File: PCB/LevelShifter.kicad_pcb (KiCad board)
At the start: 2 copper layers, 122.7 x 104.9 mm, 110 parts, among them J1 POWER, J10 M2, J11 M1, J12 Selector, J13 M0, J14 M_FEED, J15 M_FEED, J16 M_FEED, J17 Selector, J18 OUTPUT, J19 OUT0, J2 INPUT, J20 OUT1, J21 OUT2, J22 OUT3, J23 IN0, J24 IN1, J25 IN2, J26 IN3, J27 ROBOT, J28 ZIF, J3 ANALOG0, J4 ANALOG1, J5 ANALOG2, J6 ANALOG3, J7 DE9_Plug_MountingHoles, J8 SPECIAL, J9 RESET, Q1 IRF540N, Q2 IRF540N, Q3 IRF540N, U1 LM324A, U10 PC817, U2 MAX232, U3 PC817, U4 PC817, U5 PC817, U6 PC817, U7 PC817, U8 PC817, U9 PC817

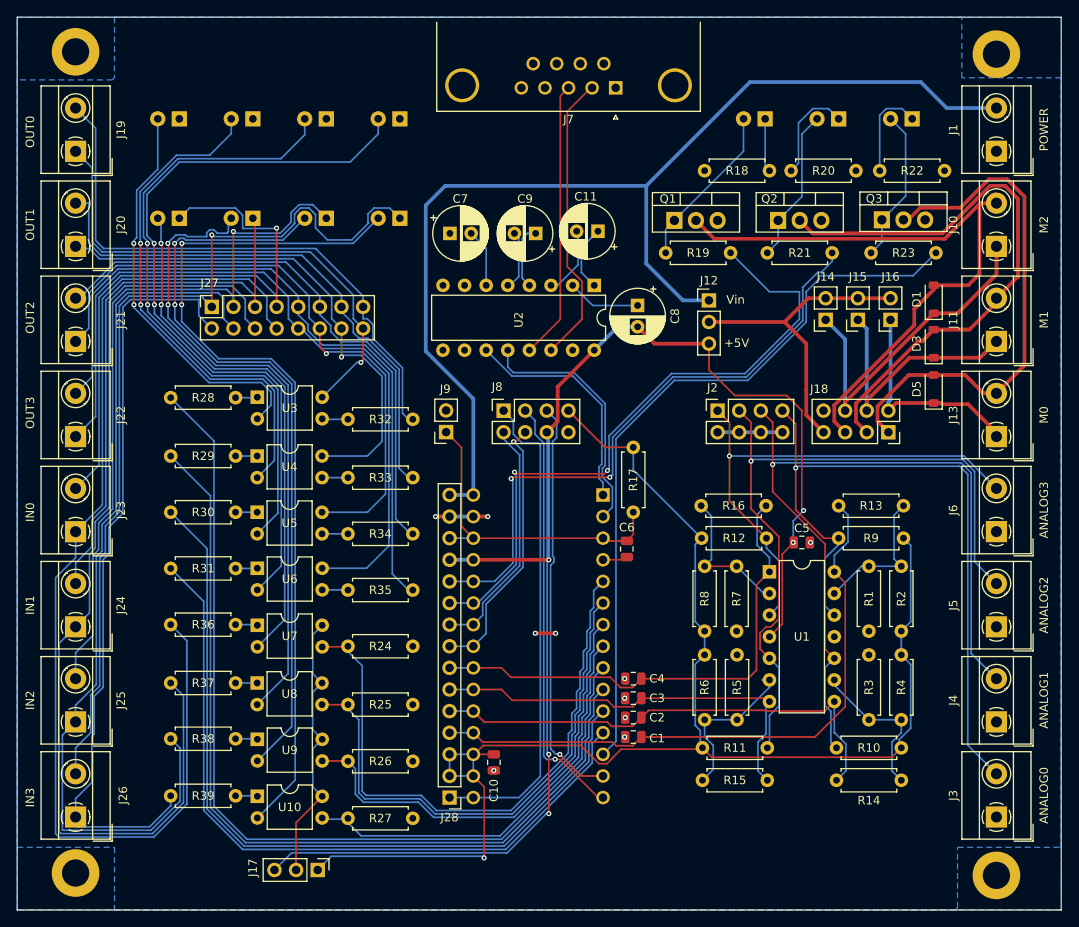
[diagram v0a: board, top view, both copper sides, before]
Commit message: [ARDUINO] Make PWM available for Servo motor (5V from buck circuit. PW on pinout) [PICO] Allow design for RaspberryPi Pico placement
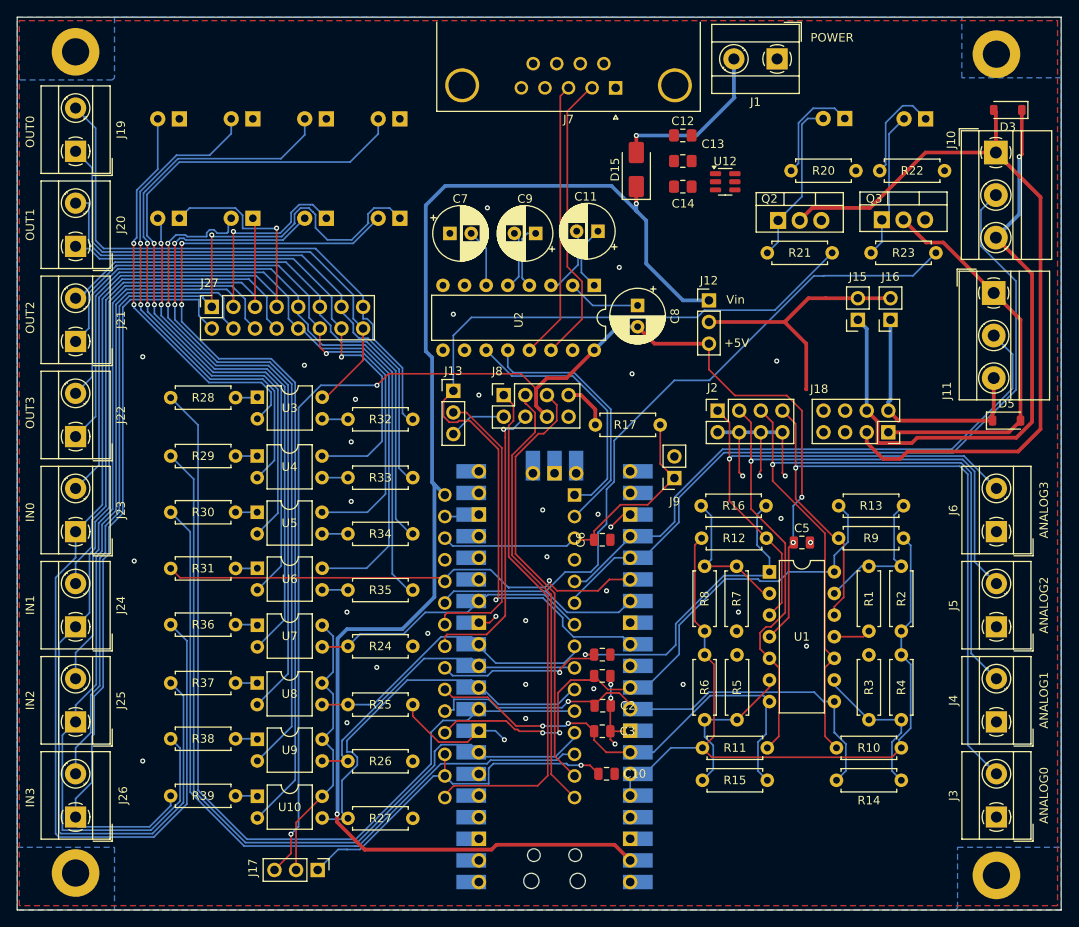
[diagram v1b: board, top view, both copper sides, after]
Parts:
- removed D1: BAV16W, Diode_SMD:D_SOD-123
- removed D2: LED, LED_THT:LED_D5.0mm
- removed J14: M_FEED, Connector_PinSocket_2.54mm:PinSocket_1x02_P2.54mm_Vertical
- removed J28: ZIF, Connector_PinHeader_2.54mm:PinHeader_1x15_P2.54mm_Vertical
- removed Q1: IRF540N, Package_TO_SOT_THT:TO-220-3_Vertical
- removed R18, R19: 22, Resistor_THT:R_Axial_DIN0207_L6.3mm_D2.5mm_P7.62mm_Horizontal
- added C12: 10uF, Capacitor_SMD:C_0805_2012Metric_Pad1.18x1.45mm_HandSolder, F.Cu at (205.5, 52.0)
- added C13: 100nF, Capacitor_SMD:C_0805_2012Metric_Pad1.18x1.45mm_HandSolder, F.Cu at (205.5, 55.0)
- added C14: 47uF, Capacitor_SMD:C_0805_2012Metric_Pad1.18x1.45mm_HandSolder, F.Cu at (205.5, 58.0)
- added D15: SS14, Diode_SMD:D_SMA, F.Cu at (200.0, 56.0)
- added U11: Pico, Components:pico, B.Cu at (190.4, 115.6)
- added U12: AP63203WU, Package_TO_SOT_SMD:TSOT-23-6, F.Cu at (210.4, 57.4)
- J10: value M2 -> Screw_Terminal_01x03; footprint TerminalBlock_MetzConnect:TerminalBlock_MetzConnect_Type101_RT01602HBWC_1x02_P5.08mm_Horizontal -> TerminalBlock_MetzConnect:TerminalBlock_MetzConnect_Type011_RT05503HBWC_1x03_P5.00mm_Horizontal
- J11: value M1 -> Screw_Terminal_01x03; footprint TerminalBlock_MetzConnect:TerminalBlock_MetzConnect_Type101_RT01602HBWC_1x02_P5.08mm_Horizontal -> TerminalBlock_MetzConnect:TerminalBlock_MetzConnect_Type011_RT05503HBWC_1x03_P5.00mm_Horizontal
- J13: value M0 -> Selector; footprint TerminalBlock_MetzConnect:TerminalBlock_MetzConnect_Type101_RT01602HBWC_1x02_P5.08mm_Horizontal -> Connector_PinHeader_2.54mm:PinHeader_1x03_P2.54mm_Vertical
- R20, R21, R22, R23: value 22 -> 150
- R28, R29, R30, R31: value 100 -> 200
- moved J13 64.0 mm to (178.5, 82.0), turned to 0 degrees
- moved D3 28.8 mm to (243.7, 49.0), turned to 180 degrees
- moved J1 28.0 mm to (216.5, 43.0), turned to 180 degrees
- moved J9 27.4 mm to (204.5, 92.2)
- moved C10 13.3 mm to (196.5, 127.0), turned to 0 degrees
- moved J10 11.0 mm to (242.2, 54.0), turned to -90 degrees
- moved D5 9.32 mm to (243.5, 85.5), turned to 0 degrees
- moved C1 8.05 mm to (196.0, 115.5), turned to 0 degrees
- moved J11 5.70 mm to (242.0, 70.5), turned to -90 degrees
- moved C3 5.33 mm to (196.0, 122.0), turned to 0 degrees
- moved R17 5.18 mm to (195.2, 86.0), turned to 0 degrees
- moved C4 4.61 mm to (196.0, 113.0), turned to 0 degrees
- moved C2 3.86 mm to (196.1, 119.0), turned to 0 degrees
- moved A1 3.35 mm to (192.7, 94.2)
- moved C6 3.08 mm to (196.0, 99.5), turned to 0 degrees
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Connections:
- A1 pad 10: /OUT1 -> /IN3
- A1 pad 11: /OUT2 -> /OUT0
- A1 pad 12: /OUT3 -> /OUT1
- A1 pad 13: /CTRL0 -> /OUT2
- A1 pad 24: /SCL -> Net-(A1-SCL/A5)
- A1 pad 25: /CTRL2 -> /CTRL0
- A1 pad 26: /CTRL1 -> /OUT3
- A1 pad 27: VCC -> unconnected-(A1-+5V-Pad27)
- A1 pad 5: /IN0 -> /PWM0
- A1 pad 6: /IN1 -> /PWM1
- A1 pad 7: /IN2 -> /IN0
- A1 pad 8: /IN3 -> /IN1
- A1 pad 9: /OUT0 -> /IN2
- J1 pad 2: Vin -> Net-(D15-A)
- J10 pad 1: Net-(D1-K) -> Net-(D3-A)
- J10 pad 2: Net-(D1-A) -> /PWM1
- J11 pad 1: Net-(D3-K) -> Net-(D5-A)
- J11 pad 2: Net-(D3-A) -> /PWM0
- J13 pad 1: Net-(D5-K) -> /CTRL1
- J13 pad 2: Net-(D5-A) -> Net-(A1-SCL/A5)
- J18 pad 5: Net-(D1-A) -> unconnected-(J18-Pin_5-Pad5)
- J18 pad 6: Net-(D1-K) -> unconnected-(J18-Pin_6-Pad6)
- J18 pad 7: Net-(J12-Pin_2) -> unconnected-(J18-Pin_7-Pad7)
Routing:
- net /PWM1: track 0.00 -> 90.0 mm
- net /CTRL2: track 77.2 -> 0.00 mm, vias 2 -> 0
- net Net-(D1-A): track 74.9 -> 0.00 mm
- net /PWM0: track 0.00 -> 69.8 mm
- net Net-(D3-K): track 30.4 -> 74.3 mm, vias 0 -> 1
- net GND: track 19.8 -> 62.4 mm, vias 10 -> 39
- net Net-(D1-K): track 39.9 -> 0.00 mm
- net /IN0: track 70.8 -> 33.7 mm
- net Vin: track 131.8 -> 166.1 mm, vias 0 -> 2
- net Net-(A1-SCL/A5): track 0.00 -> 34.0 mm
- net VCCQ: track 173.2 -> 139.5 mm
- net /CTRL1: track 72.5 -> 103.2 mm, vias 2 -> 1
- net /IN1: track 62.4 -> 35.4 mm
- net /OUT3: track 85.9 -> 59.3 mm, vias 0 -> 1
- net /SCL: track 29.2 -> 6.76 mm
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- added copper zone on F.Cu, net GND

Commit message: [UPDATE] outing done. Start the final touch!
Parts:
- added J14: Serial, Connector_PinSocket_2.54mm:PinSocket_1x04_P2.54mm_Vertical, F.Cu at (178.9, 53.5)
- moved C13 7.14 mm to (208.5, 61.5), turned to -90 degrees
- moved C14 7.01 mm to (206.0, 65.0), turned to 180 degrees
- moved U12 6.40 mm to (205.5, 61.5), turned to -90 degrees
- moved C12 6.01 mm to (205.5, 58.0)
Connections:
- J18 pad 5: unconnected-(J18-Pin_5-Pad5) -> /PWM1
- J18 pad 6: unconnected-(J18-Pin_6-Pad6) -> /PWM0
- U11 pad 1: unconnected-(U11-GPIO0-Pad1) -> Net-(A1-TX1)
- U11 pad 19: unconnected-(U11-GPIO14-Pad19) -> /SDA
- U11 pad 2: unconnected-(U11-GPIO1-Pad2) -> Net-(A1-RX1)
- U11 pad 20: unconnected-(U11-GPIO15-Pad20) -> /SCL
- U11 pad 22: unconnected-(U11-GPIO17-Pad22) -> /PWM0
- U11 pad 24: /PWM0 -> /PWM1
- U11 pad 25: /PWM1 -> /OUT2
- U11 pad 4: unconnected-(U11-GPIO2-Pad4) -> /SCK
- U11 pad 5: unconnected-(U11-GPIO3-Pad5) -> /MOSI
- U11 pad 6: /OUT2 -> /MISO
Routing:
- net Net-(A1-TX1): track 29.8 -> 111.5 mm, vias 0 -> 1
- net Net-(A1-RX1): track 30.5 -> 108.2 mm, vias 0 -> 1
- net VCCQ: track 139.5 -> 171.7 mm
- net /OUT2: track 86.1 -> 113.3 mm, vias 0 -> 2
- net VCC: track 157.9 -> 180.5 mm
- net /MOSI: track 50.5 -> 66.0 mm
- net /MISO: track 52.0 -> 66.1 mm, vias 0 -> 1
- net GND: track 62.4 -> 73.5 mm, vias 39 -> 52
- net Net-(J12-Pin_2): track 31.5 -> 22.5 mm
- net /PWM0: track 69.8 -> 76.2 mm
- net /SCL: track 6.76 -> 12.4 mm
- net Net-(U12-SW): track 0.00 -> 4.30 mm
- net /SDA: track 34.4 -> 37.9 mm, vias 1 -> 2
- net /SCK: track 60.7 -> 63.9 mm
- net Vin: track 166.1 -> 169.0 mm, vias 2 -> 1
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
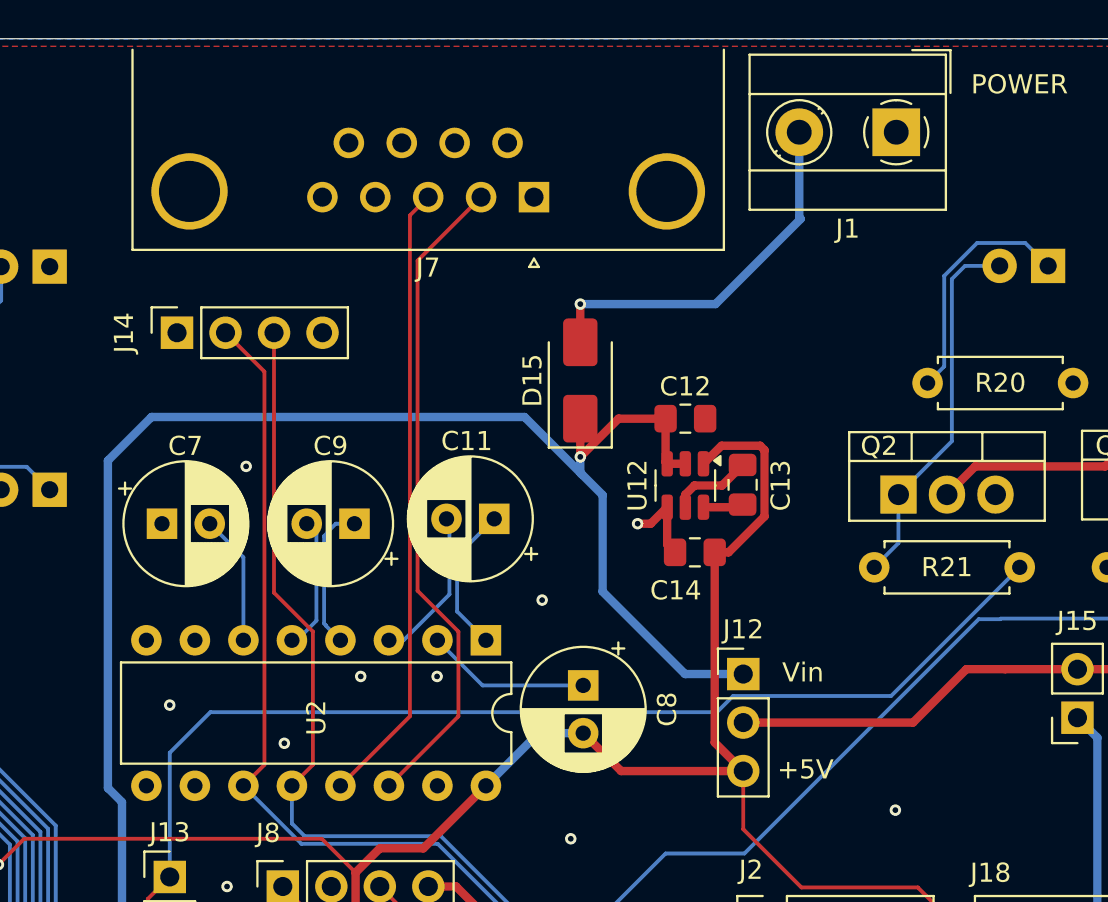
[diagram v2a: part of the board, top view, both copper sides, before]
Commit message: [COMPLETED] All tracks laid. Wiaitng for the production of the PCB.
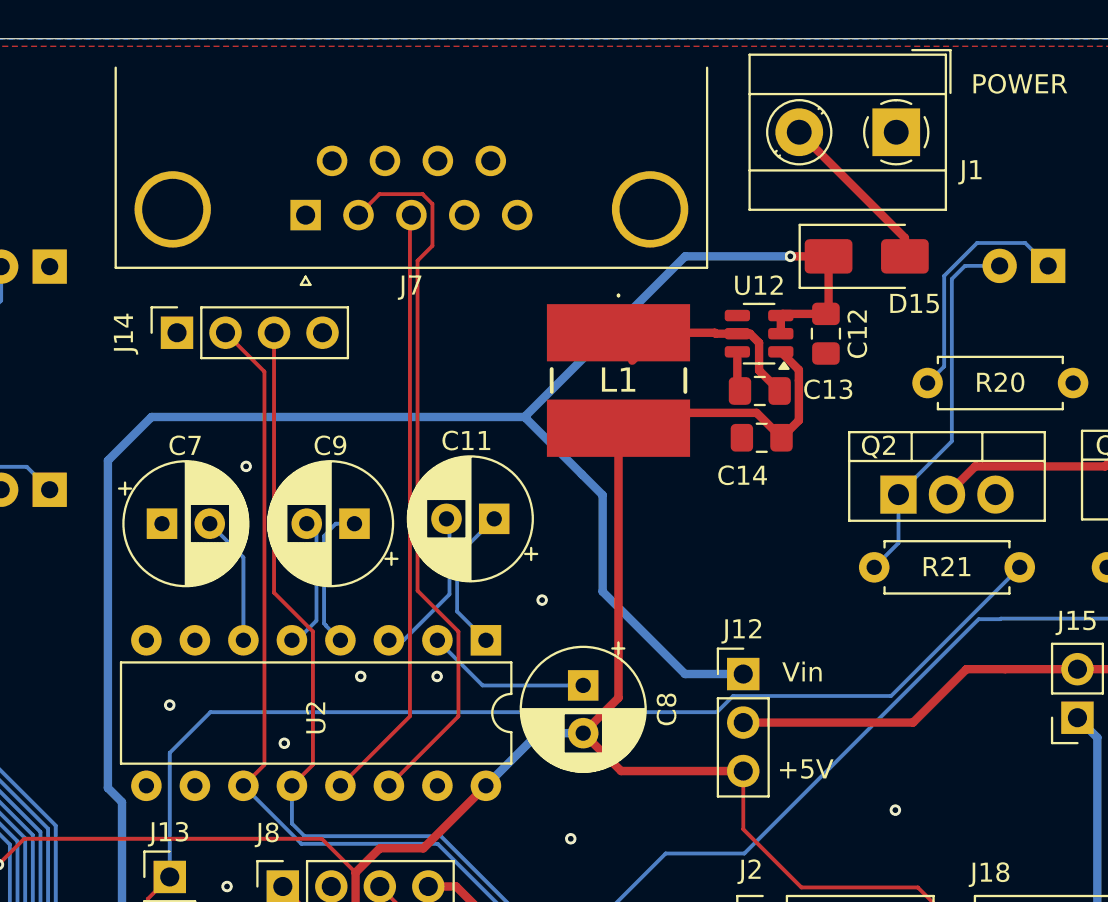
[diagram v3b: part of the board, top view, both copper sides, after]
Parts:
- added L1: 74404052039, Components:CD75, F.Cu at (202.0, 56.0)
- J7: footprint Connector_Dsub:DSUB-9_Male_Horizontal_P2.77x2.84mm_EdgePinOffset4.94mm_Housed_MountingHolesOffset7.48mm -> Connector_Dsub:DSUB-9_Female_Horizontal_P2.77x2.84mm_EdgePinOffset4.94mm_Housed_MountingHolesOffset7.48mm
- moved D15 16.3 mm to (215.0, 49.5), turned to 0 degrees
- moved J7 12.0 mm to (185.6, 47.3)
- moved U12 8.84 mm to (209.4, 53.5), turned to 180 degrees
- moved C12 8.60 mm to (212.9, 53.5), turned to -90 degrees
- moved C14 6.95 mm to (209.5, 59.0)
- moved C13 4.99 mm to (209.4, 56.5), turned to 180 degrees
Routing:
- net Vin: track 169.0 -> 183.2 mm
- net Net-(D15-A): track 20.0 -> 8.79 mm, vias 1 -> 0
- net VCC: track 180.5 -> 189.3 mm
- net Net-(U12-SW): track 4.30 -> 12.6 mm
- net GND: track 73.5 -> 69.0 mm, vias 52 -> 51
- net Net-(U2-T1OUT): track 34.6 -> 37.7 mm
- net Net-(U2-R1IN): track 32.7 -> 31.4 mm

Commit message: [TESTED]
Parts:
- added J28: M_FEED, Connector_PinSocket_2.54mm:PinSocket_1x02_P2.54mm_Vertical, F.Cu at (222.0, 73.7)
- C11, C7, C8, C9: value C_Polarized -> 1uF; footprint Capacitor_THT:CP_Radial_D6.3mm_P2.50mm -> Capacitor_SMD:C_1206_3216Metric_Pad1.33x1.80mm_HandSolder
- C12, C14: footprint Capacitor_SMD:C_0805_2012Metric_Pad1.18x1.45mm_HandSolder -> Capacitor_SMD:C_1206_3216Metric_Pad1.33x1.80mm_HandSolder
- moved C4 24.6 mm to (174.0, 102.0), turned to 180 degrees
- moved J12 8.47 mm to (217.0, 71.2)
- moved C3 8.29 mm to (204.1, 124.0)
- moved C1 8.06 mm to (204.0, 116.5)
- moved C2 7.97 mm to (204.0, 119.5)
- moved C11 4.42 mm to (192.5, 66.5)
- moved C9 3.44 mm to (186.5, 66.5)
- moved C7 3.12 mm to (178.9, 66.5)
- moved C6 3.03 mm to (196.4, 96.5)
- moved C8 1.74 mm to (198.5, 72.5), turned to 90 degrees
- moved C12 0.78 mm to (213.5, 54.0)
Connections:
- A1 pad 19: /ANALOG0 -> /OUT3
- A1 pad 20: /ANALOG1 -> /CTRL0
- A1 pad 22: /ANALOG3 -> /ANALOG1
- A1 pad 25: /CTRL0 -> /ANALOG0
- A1 pad 26: /OUT3 -> /ANALOG3
- A1 pad 5: /PWM0 -> /IN0
- A1 pad 6: /PWM1 -> /IN1
- A1 pad 7: /IN0 -> /IN2
- A1 pad 8: /IN1 -> /PWM0
- A1 pad 9: /IN2 -> /PWM1
- C8 pad 1: Net-(U2-VS+) -> VCC
- C8 pad 2: VCC -> Net-(U2-VS+)
- U11 pad 39: Vin -> VCC
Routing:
- net VCC: track 189.3 -> 324.5 mm, vias 4 -> 5
- net Vin: track 183.2 -> 101.1 mm
- net /OUT3: track 61.0 -> 107.4 mm
- net /CTRL0: track 93.4 -> 121.5 mm, vias 0 -> 3
- net GND: track 69.0 -> 42.1 mm, vias 51 -> 50
- net /PWM0: track 76.2 -> 86.2 mm
- net /OUT2: track 113.3 -> 122.9 mm
- net /PWM1: track 92.6 -> 101.6 mm
- net Net-(J12-Pin_2): track 22.5 -> 13.9 mm
- net /ANALOG0: track 69.0 -> 77.5 mm
- net Net-(U2-T1OUT): track 37.7 -> 31.4 mm, vias 0 -> 1
- net /ANALOG2: track 56.4 -> 62.6 mm, vias 2 -> 0
- net /CTRL1: track 103.2 -> 108.5 mm
- net Net-(U2-C1-): track 8.19 -> 3.50 mm
- net Net-(U2-C2+): track 7.69 -> 3.37 mm
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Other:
- board text added: "+3.3V"
- board text added: "CTRL1"
- board text added: "LevelShifter V3.0 [Arduino NANO] OR [PICO]"
- board text added: "SCL"
